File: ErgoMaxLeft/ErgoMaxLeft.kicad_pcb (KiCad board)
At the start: 2 copper layers, 182.8 x 169.2 mm, 102 parts, among them J1 PJ-320A, K1 KEYSW, K10 KEYSW, K11 KEYSW, K12 KEYSW, K13 KEYSW, K14 KEYSW, K15 KEYSW, K16 KEYSW, K17 KEYSW, K18 KEYSW, K19 KEYSW, K2 KEYSW, K20 KEYSW, K21 KEYSW, K22 KEYSW, K23 KEYSW, K24 KEYSW, K25 KEYSW, K26 KEYSW, K27 KEYSW, K28 KEYSW, K29 KEYSW, K3 KEYSW, K30 KEYSW, K31 KEYSW, K32 KEYSW, K33 KEYSW, K34 KEYSW, K35 KEYSW, K36 KEYSW, K37 KEYSW, K38 KEYSW, K39 KEYSW, K4 KEYSW, K40 KEYSW, K41 KEYSW, K42 KEYSW, K43 KEYSW, K44 KEYSW, K5 KEYSW, K6 KEYSW, K7 KEYSW, K8 KEYSW, K9 KEYSW, U1 ProMicro

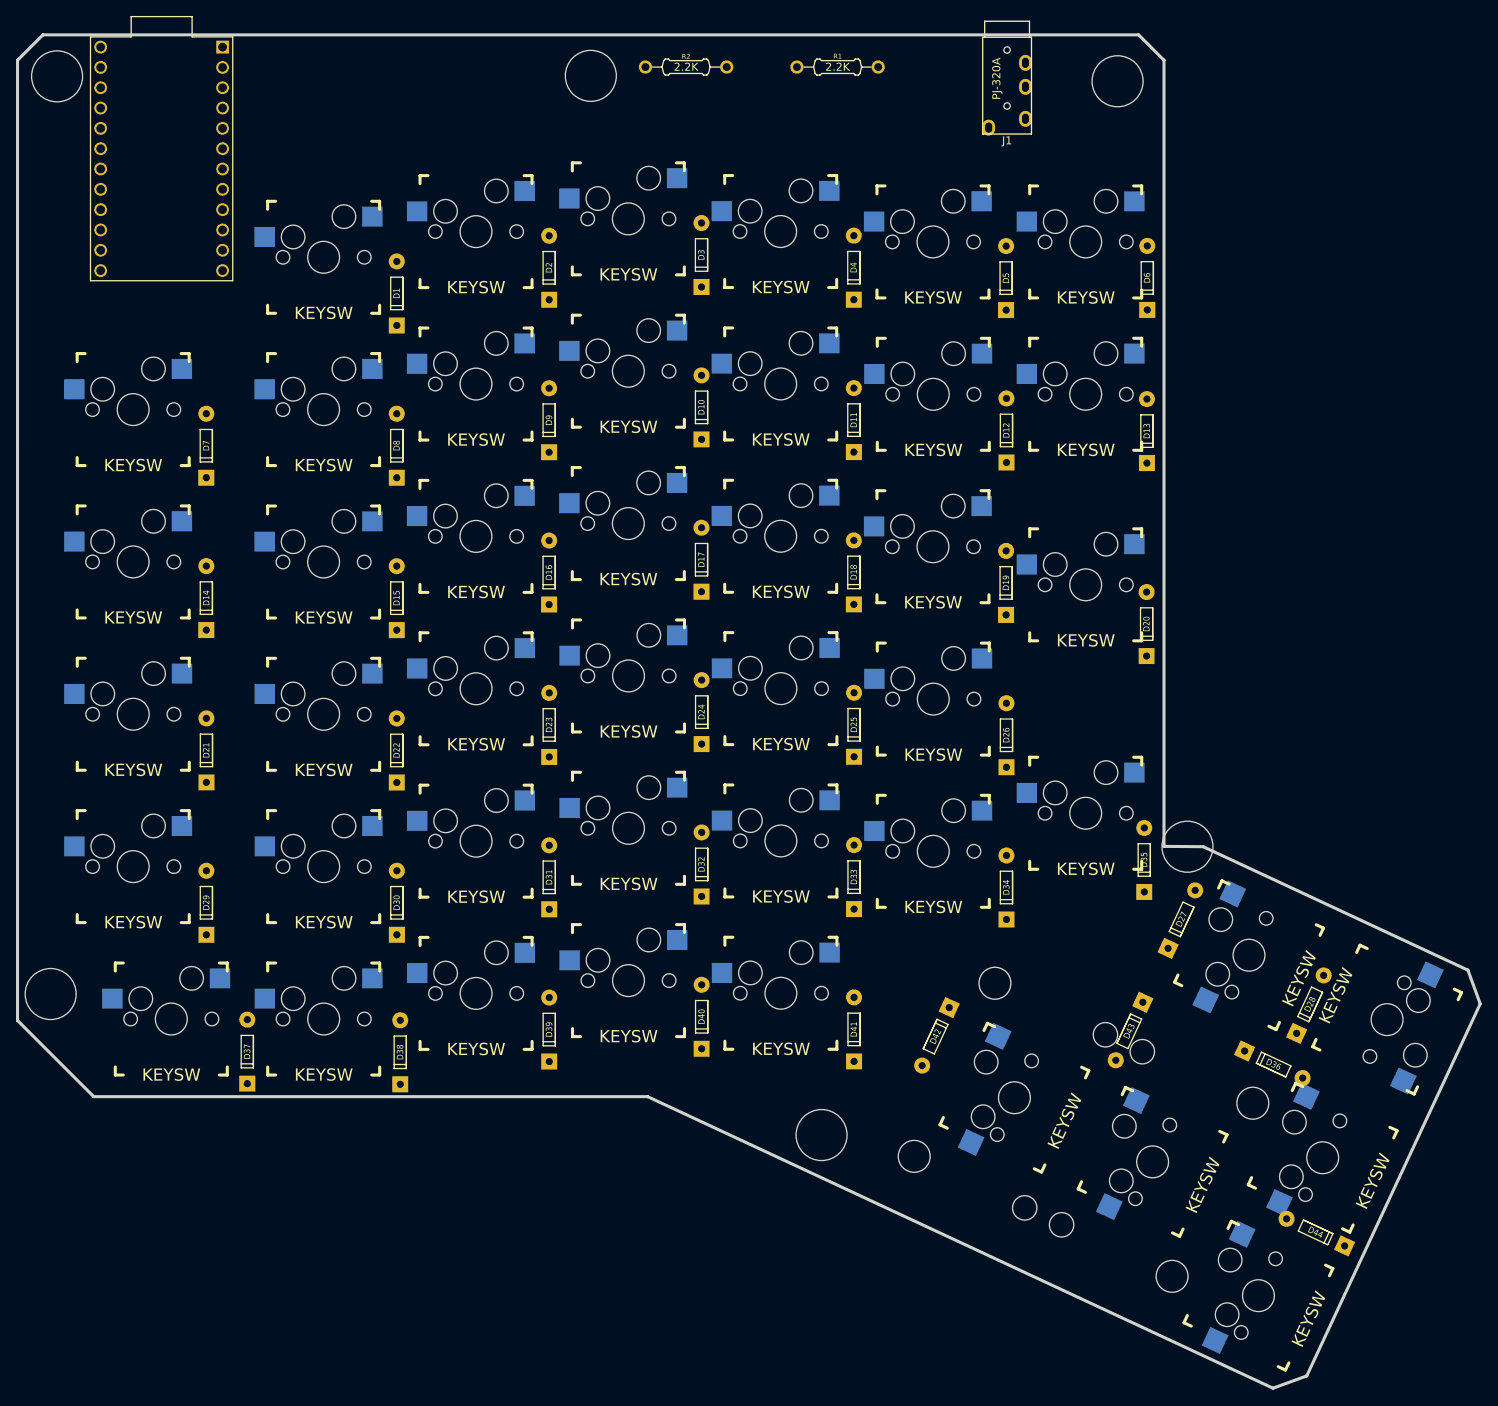
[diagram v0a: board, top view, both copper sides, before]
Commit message: move last components to other side of the PCB
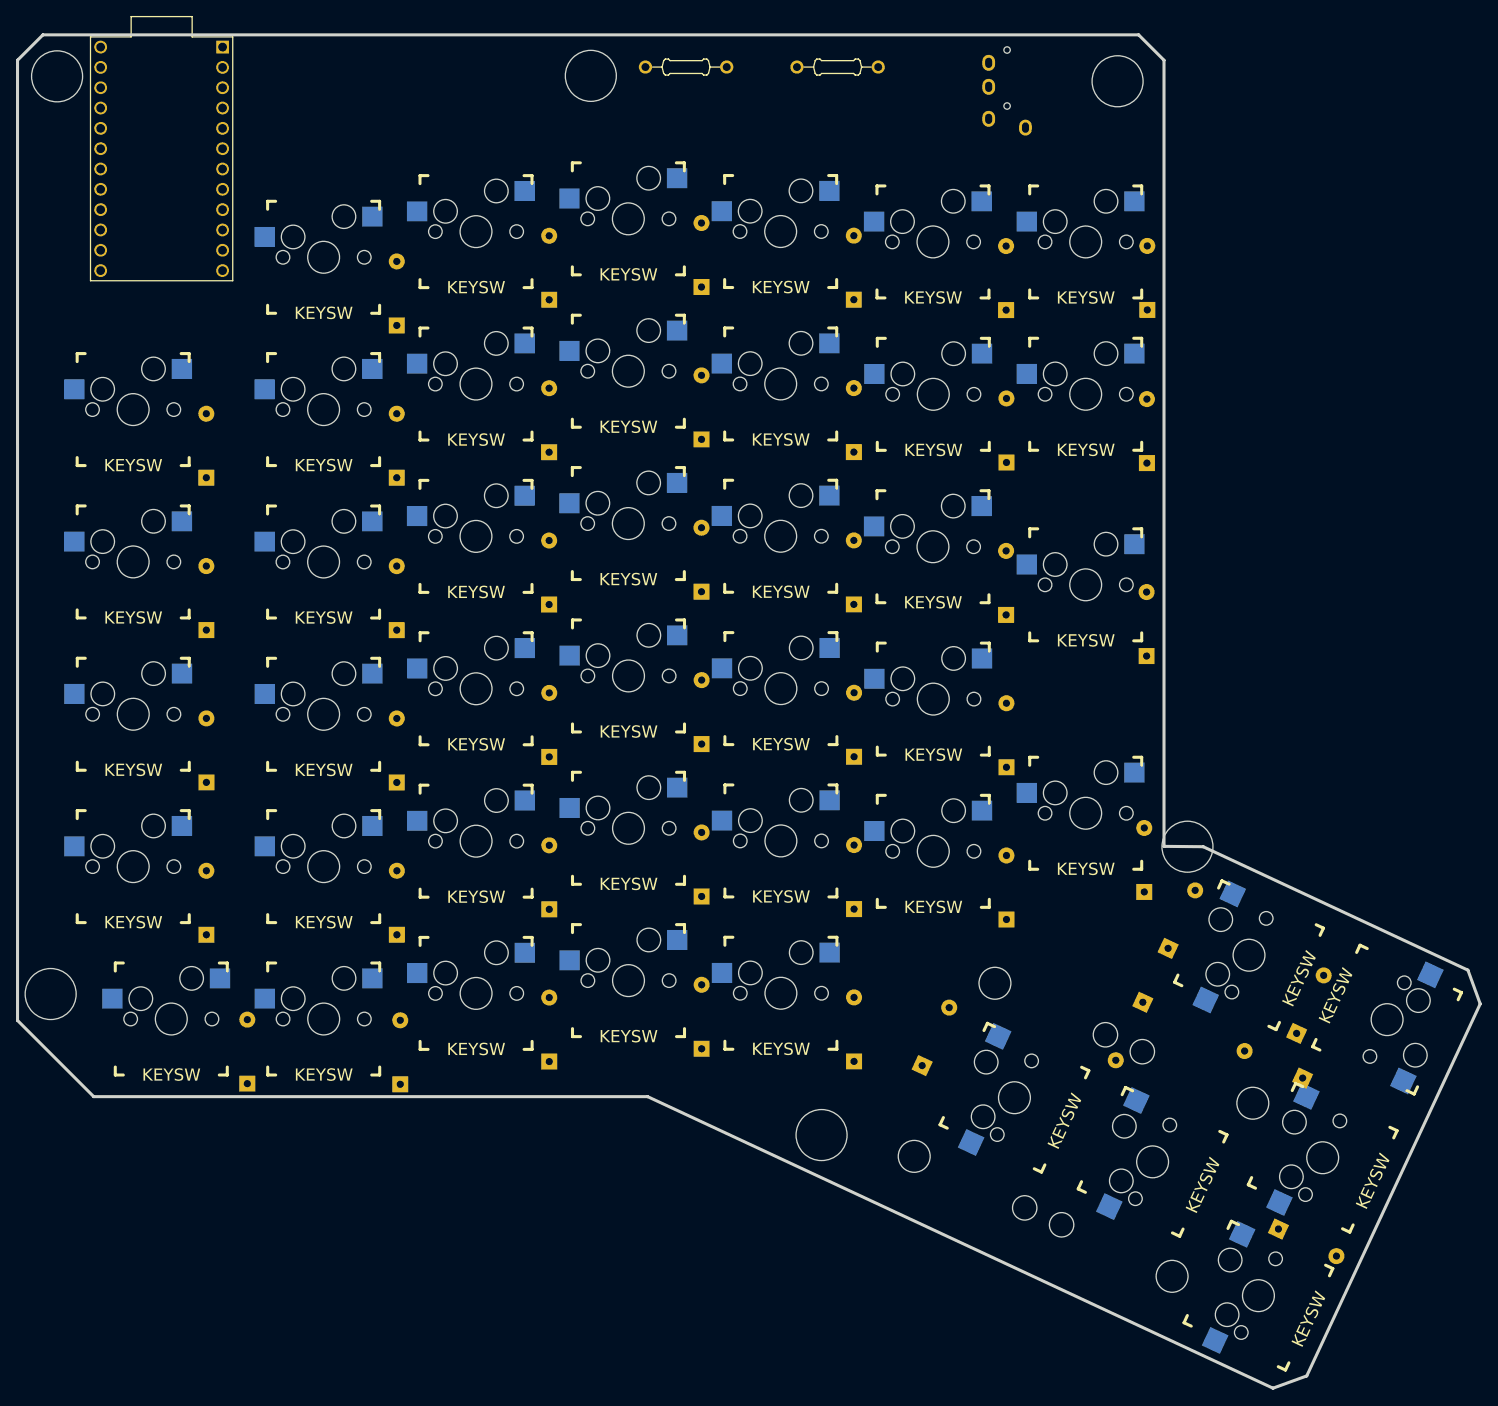
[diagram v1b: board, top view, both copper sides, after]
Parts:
- D1, D10, D11, D12, D13, D14, D15, D16, D17, D18, D19, D2, D20, D21, D22, D23, D24, D25, D26, D27, D28, D29, D3, D30, D31, D32, D33, D34, D35, D36, D37, D38, D39, D4, D40, D41, D42, D43, D44, D5, D6, D7, D8, D9, J1, R1, R2: moved to B.Cu
- moved D44 1.64 mm to (271.6, 186.8), turned to 155 degrees
- turned D36 to 335 degrees
- turned D42 to 245 degrees
- turned J1 to 180 degrees
- turned R1 to 0 degrees
- turned R2 to 0 degrees

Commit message: move diodes to other side of switches; add rough wiring for rows
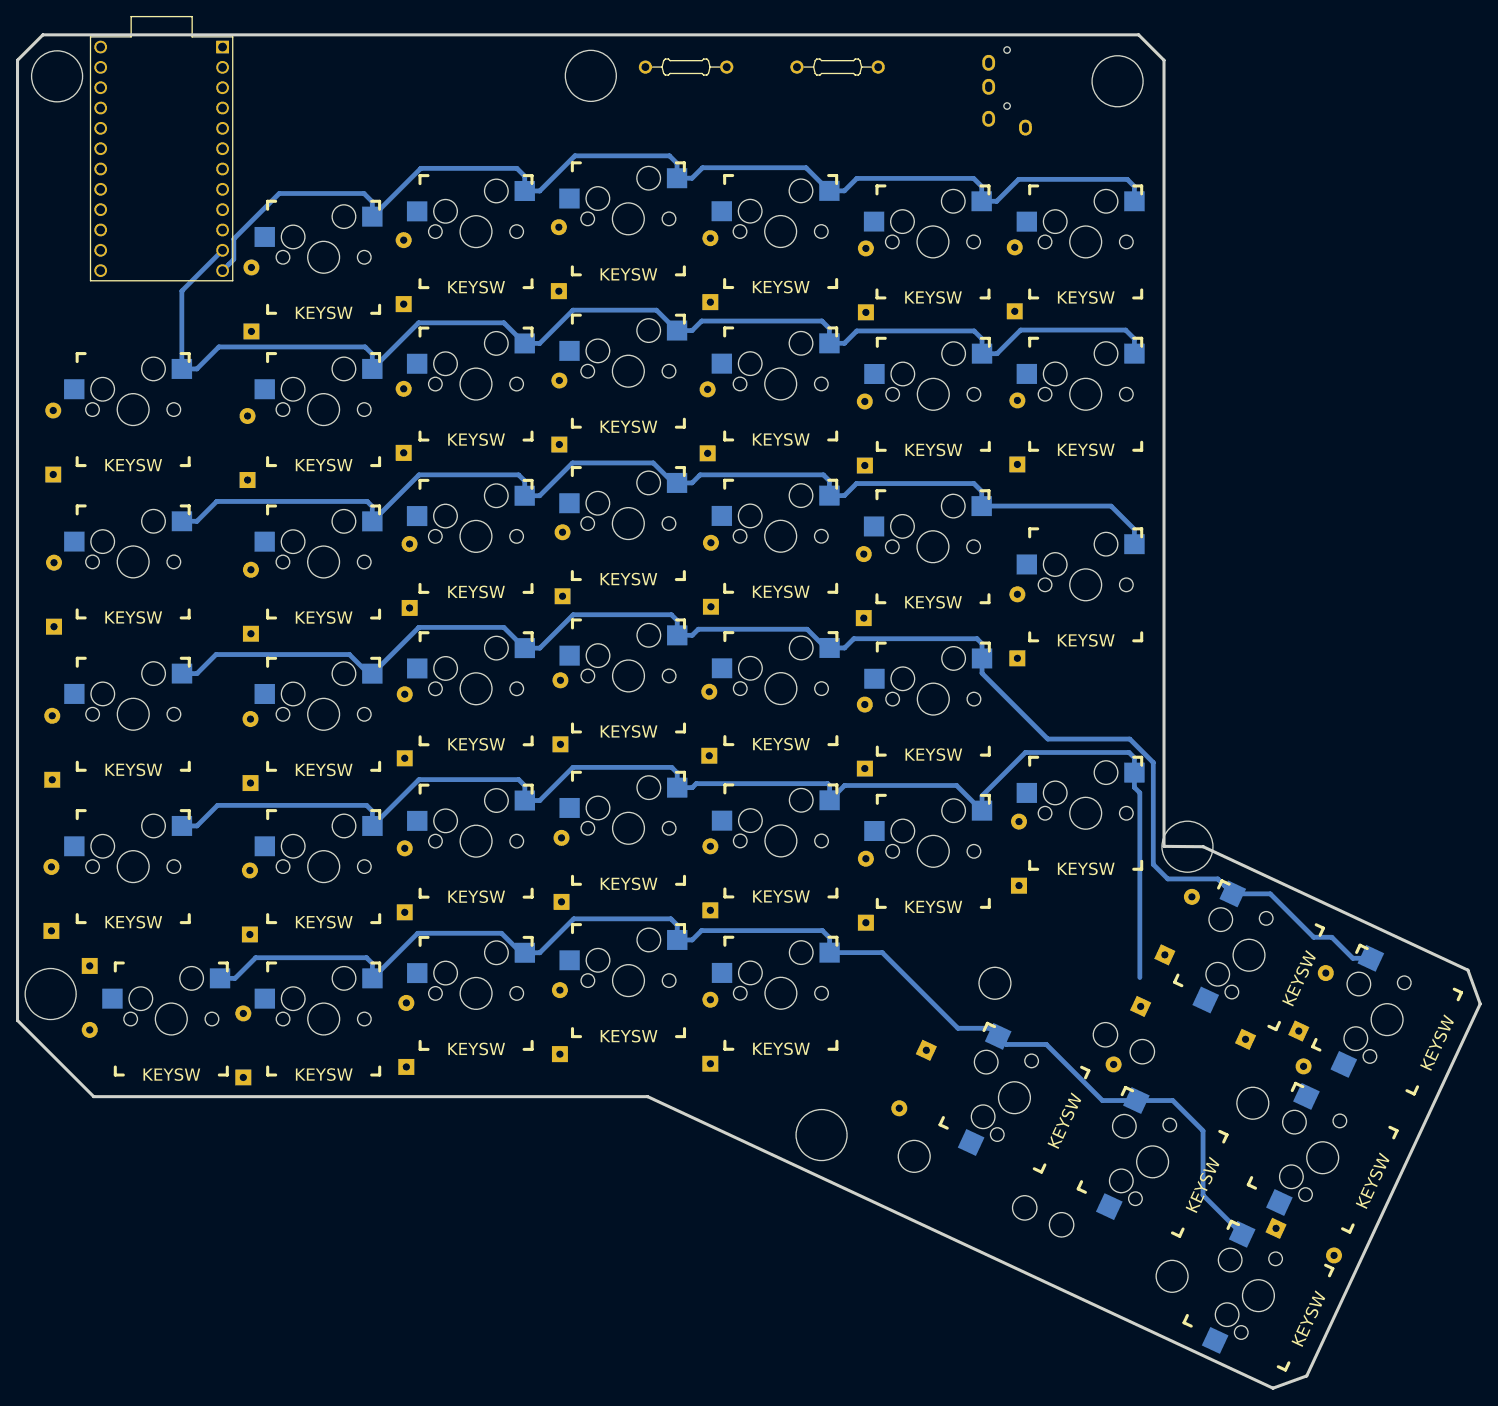
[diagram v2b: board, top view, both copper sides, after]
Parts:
- moved D37 20.8 mm to (119.4, 156.2), turned to 90 degrees
- moved D38 19.6 mm to (138.6, 162.2)
- moved D29 19.4 mm to (114.6, 143.9)
- moved D21 19.3 mm to (114.7, 125.0)
- moved D7 19.1 mm to (114.8, 86.8)
- moved D14 19.0 mm to (114.9, 105.8)
- moved D8 18.7 mm to (139.1, 87.5)
- moved D30 18.4 mm to (139.4, 144.3)
- moved D22 18.3 mm to (139.5, 125.4)
- moved D11 18.3 mm to (196.6, 84.2)
- moved D15 18.2 mm to (139.5, 106.7)
- moved D2 18.2 mm to (158.6, 65.5)
- moved D9 18.2 mm to (158.6, 84.1)
- moved D1 18.2 mm to (139.6, 68.9)
- moved D25 18.1 mm to (196.8, 122.0)
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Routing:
- net /Row3: track 0.00 -> 185.9 mm
- net /Row4: track 0.00 -> 167.0 mm
- net /Row5: track 0.00 -> 160.3 mm
- net /Row1: track 0.00 -> 154.8 mm
- net /Row0: track 0.00 -> 138.6 mm
- net /Row2: track 0.00 -> 138.0 mm
